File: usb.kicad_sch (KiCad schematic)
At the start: 8 parts

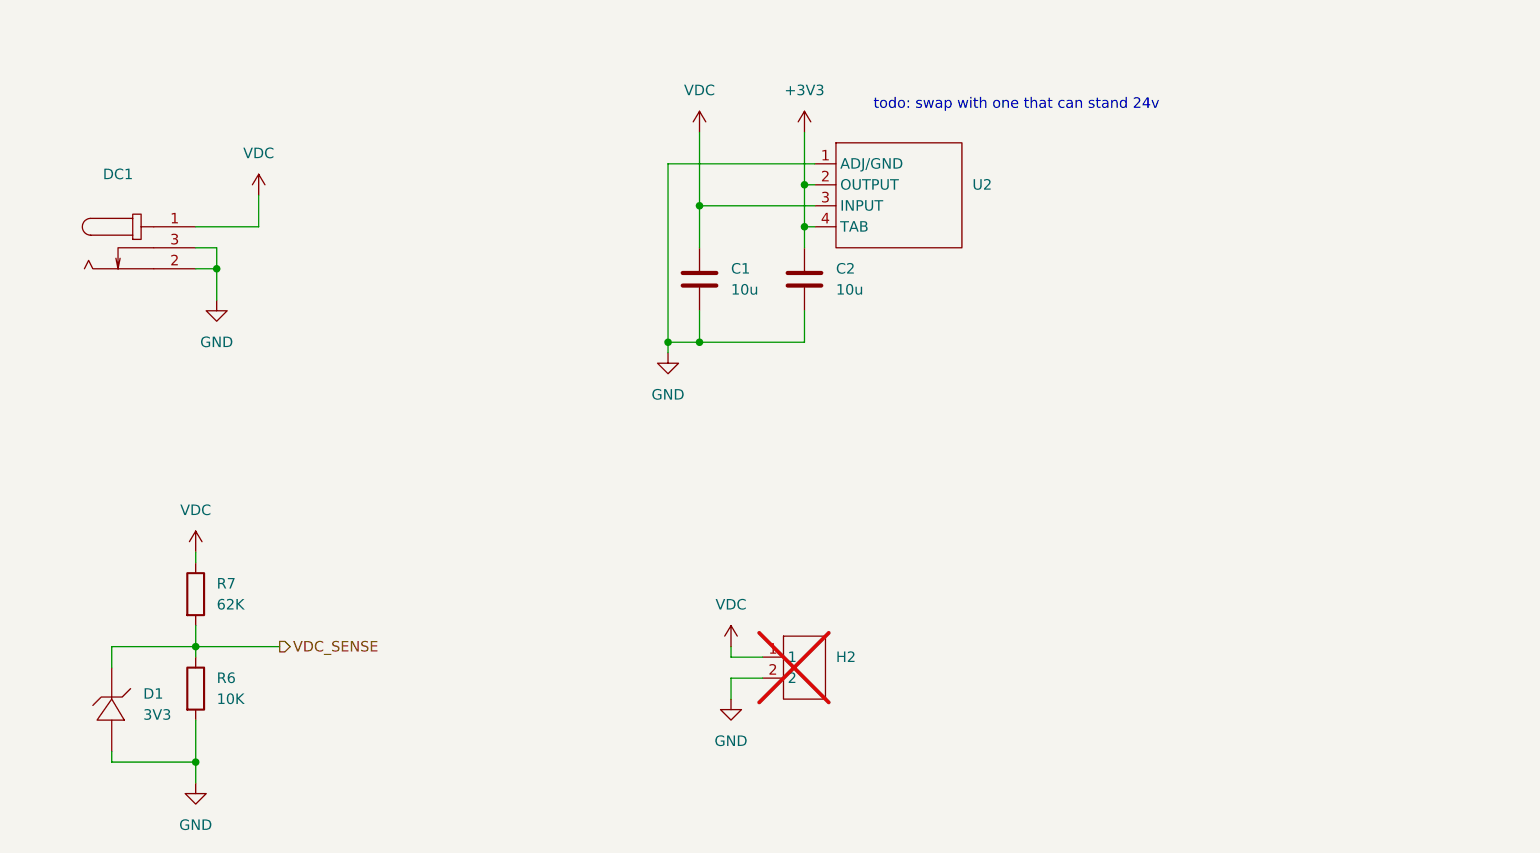
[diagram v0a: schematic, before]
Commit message: Finished the power, USB and ESP32 parts of the schematic
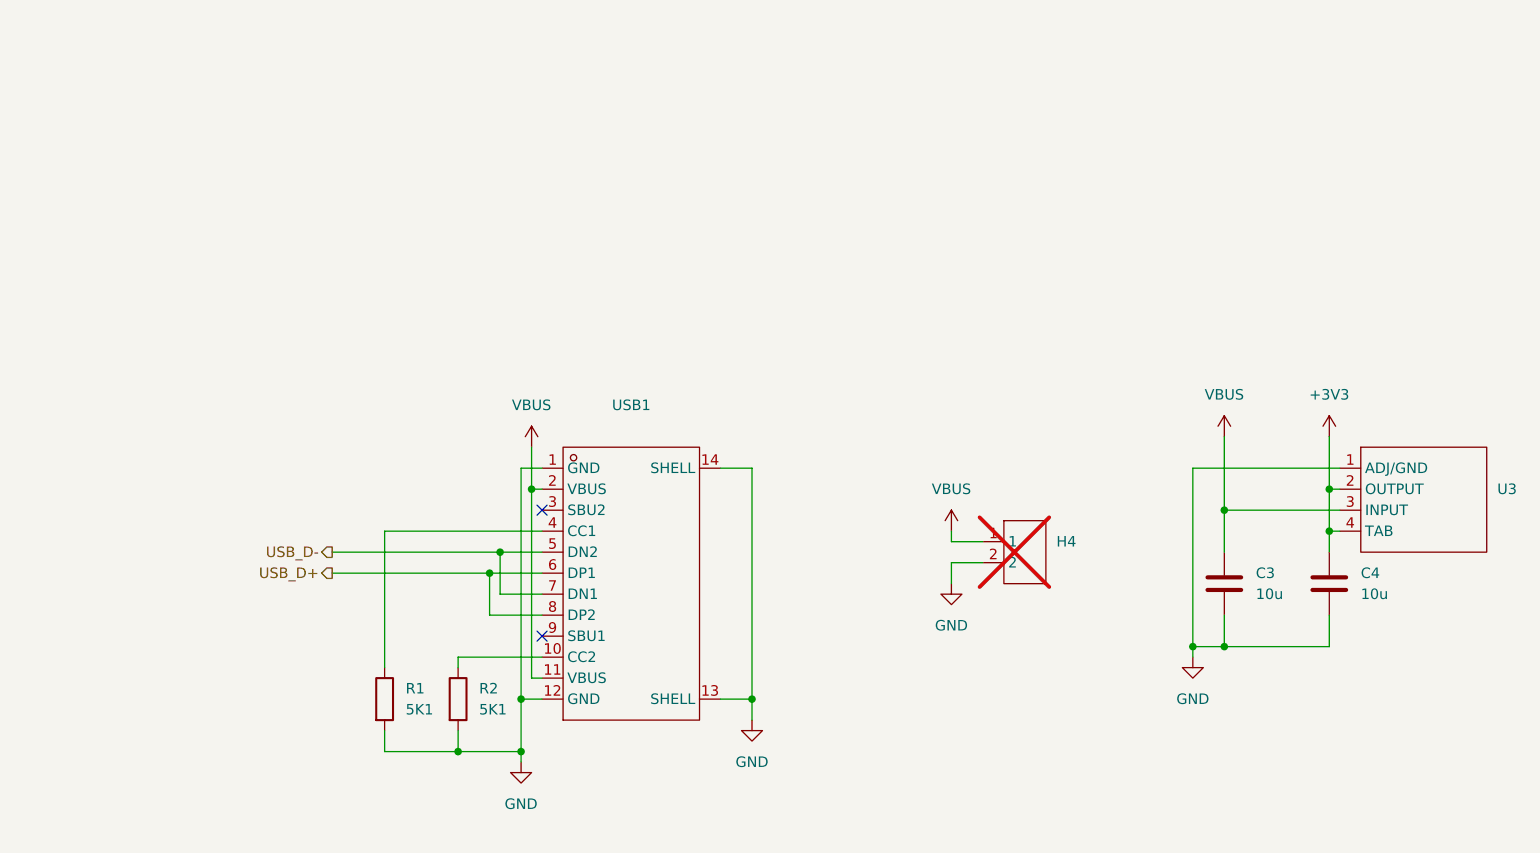
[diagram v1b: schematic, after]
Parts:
- removed C1, C2: 10u, Capacitor_SMD:C_0603_1608Metric, symbol Device:C
- removed D1: 3V3, EasyEDA_Lib:SOD-123_L2.7-W1.6-LS3.7-RD, symbol EasyEDA_Lib:BZT52C3V3
- removed DC1: ~, EasyEDA_Lib:DC-IN-TH_DC-005-A200, symbol EasyEDA_Lib:DC-005-A200
- removed H2: ~, EasyEDA_Lib:HDR-TH_2P-P2.54-V-M, symbol EasyEDA_Lib:PZ254V-11-02P
- removed R6: 10K, Resistor_SMD:R_0603_1608Metric, symbol Device:R
- removed R7: 62K, Resistor_SMD:R_0603_1608Metric, symbol Device:R
- removed U2: ~, EasyEDA_Lib:SOT-223-3_L6.5-W3.4-P2.30-LS7.0-BR, symbol EasyEDA_Lib:NCP1117ST33T3G
- added C3, C4: 10u, Capacitor_SMD:C_0603_1608Metric, symbol Device:C
- added H4: ~, EasyEDA_Lib:HDR-TH_2P-P2.54-V-M, symbol EasyEDA_Lib:PZ254V-11-02P
- added R1, R2: 5K1, Resistor_SMD:R_0603_1608Metric, symbol Device:R
- added U3: ~, EasyEDA_Lib:SOT-223-3_L6.5-W3.4-P2.30-LS7.0-BR, symbol EasyEDA_Lib:NCP1117ST33T3G
- added USB1: ~, EasyEDA_Lib:USB-C-SMD_TYPE-C-6PIN-2MD-073, symbol EasyEDA_Lib:TYPE-C 16PIN 2MD(073)
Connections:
- net +3V3: now also C4.1, U3.2 (OUTPUT), U3.4 (TAB)
- net GND: now also C3.2, C4.2, H4.2, R1.2, R2.2, U3.1 (ADJ/GND), USB1.1 (GND), USB1.12 (GND), USB1.13 (SHELL), USB1.14 (SHELL)
- new net: R1.1, USB1.4 (CC1)
- new net: R2.1, USB1.10 (CC2)
- new net USB_D+: USB1.6 (DP1), USB1.8 (DP2)
- new net USB_D-: USB1.5 (DN2), USB1.7 (DN1)
- new net VBUS: C3.1, H4.1, U3.3 (INPUT), USB1.11 (VBUS), USB1.2 (VBUS)
- no-connect marks 0 -> 2
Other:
- note removed: "todo: swap with one that can stand 24v"

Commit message: Finished schematics, started component placement
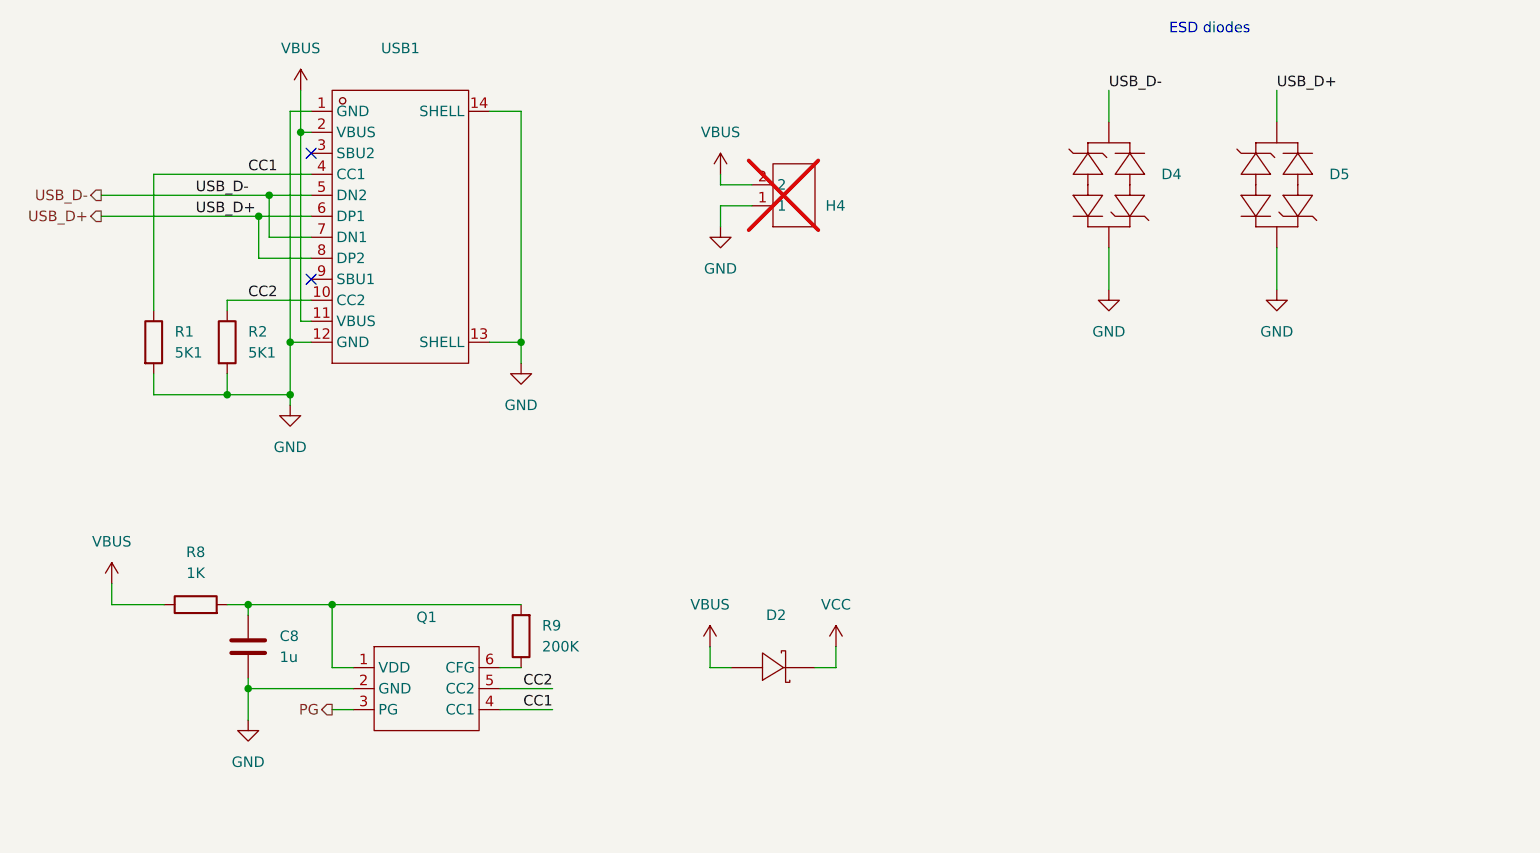
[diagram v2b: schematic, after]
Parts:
- removed C3, C4: 10u, Capacitor_SMD:C_0603_1608Metric, symbol Device:C
- removed U3: ~, EasyEDA_Lib:SOT-223-3_L6.5-W3.4-P2.30-LS7.0-BR, symbol EasyEDA_Lib:NCP1117ST33T3G
- added C8: 1u, Capacitor_SMD:C_0603_1608Metric, symbol Device:C
- added D2: ~, EasyEDA_Lib:SMA_L4.4-W2.6-LS5.0-RD, symbol EasyEDA_Lib:B340A-13-F
- added D4, D5: ~, EasyEDA_Lib:SOD-323_L1.8-W1.3-LS2.5-BI, symbol EasyEDA_Lib:PTVSUC3D5VB
- added Q1: ~, EasyEDA_Lib:SOT-23-6_L2.9-W1.6-P0.95-LS2.8-BL-2, symbol EasyEDA_Lib:CH221K
- added R8: 1K, Resistor_SMD:R_0603_1608Metric, symbol Device:R
- added R9: 200K, Resistor_SMD:R_0603_1608Metric, symbol Device:R
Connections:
- net GND: now also H4.1, C8.2, D4.1, D5.1, Q1.2 (GND); no longer H4.2
- net USB_D+: now also D5.2
- net USB_D-: now also D4.2
- net VBUS: now also H4.2, D2.2 (A), R8.1; no longer H4.1
- net CC1: now reaches R1.1, USB1.4 (CC1)
- net CC1: now also Q1.4 (CC1)
- net CC2: now reaches R2.1, USB1.10 (CC2)
- net CC2: now also Q1.5 (CC2)
- new net: C8.1, Q1.1 (VDD), R8.2, R9.2
- new net: Q1.6 (CFG), R9.1
- new net PG: Q1.3 (PG)
- new net VCC: D2.1 (K)
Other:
- note added: "ESD diodes"
- moved on the sheet: H4, R1, USB1
